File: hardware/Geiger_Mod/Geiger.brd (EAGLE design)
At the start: 52.1 x 28.6 mm, 19 parts, among them Q1 KSP44, Q2 2N3904

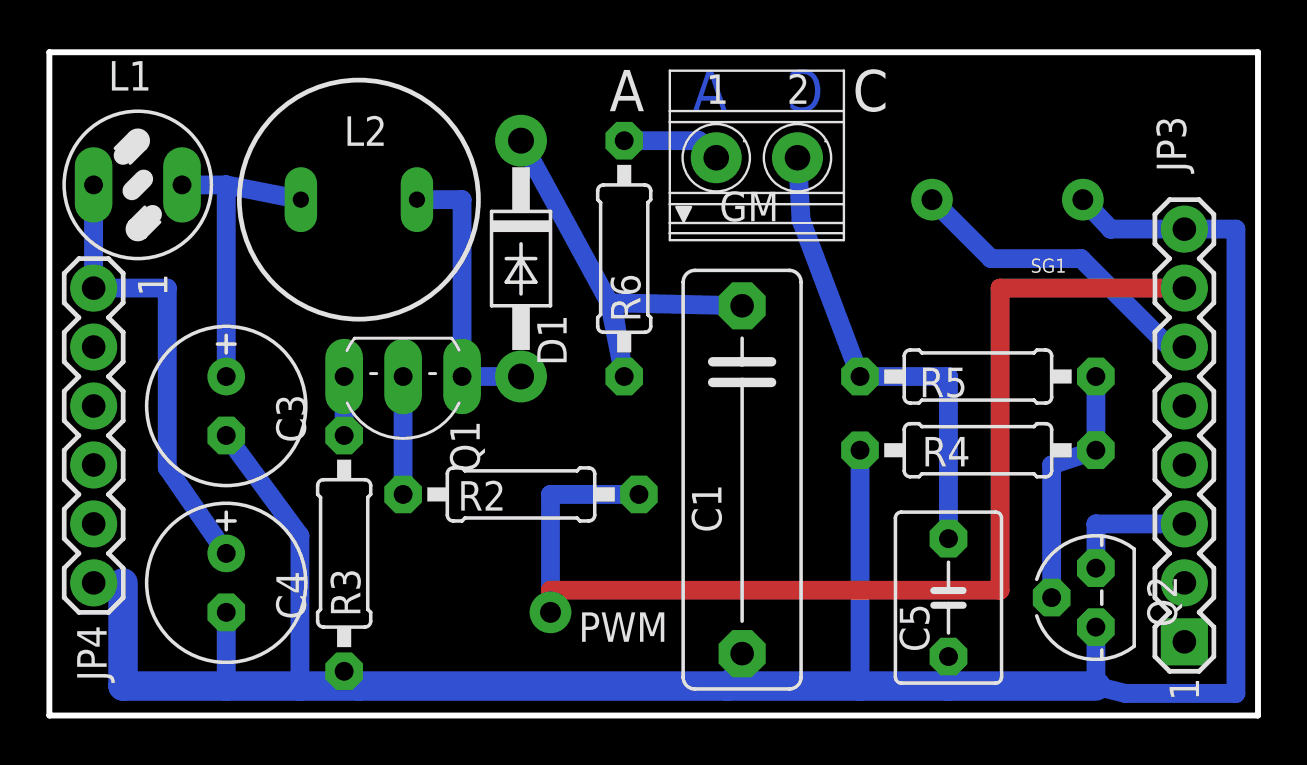
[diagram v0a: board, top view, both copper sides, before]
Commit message: Fixed Silk Screen for Q1 being wrong
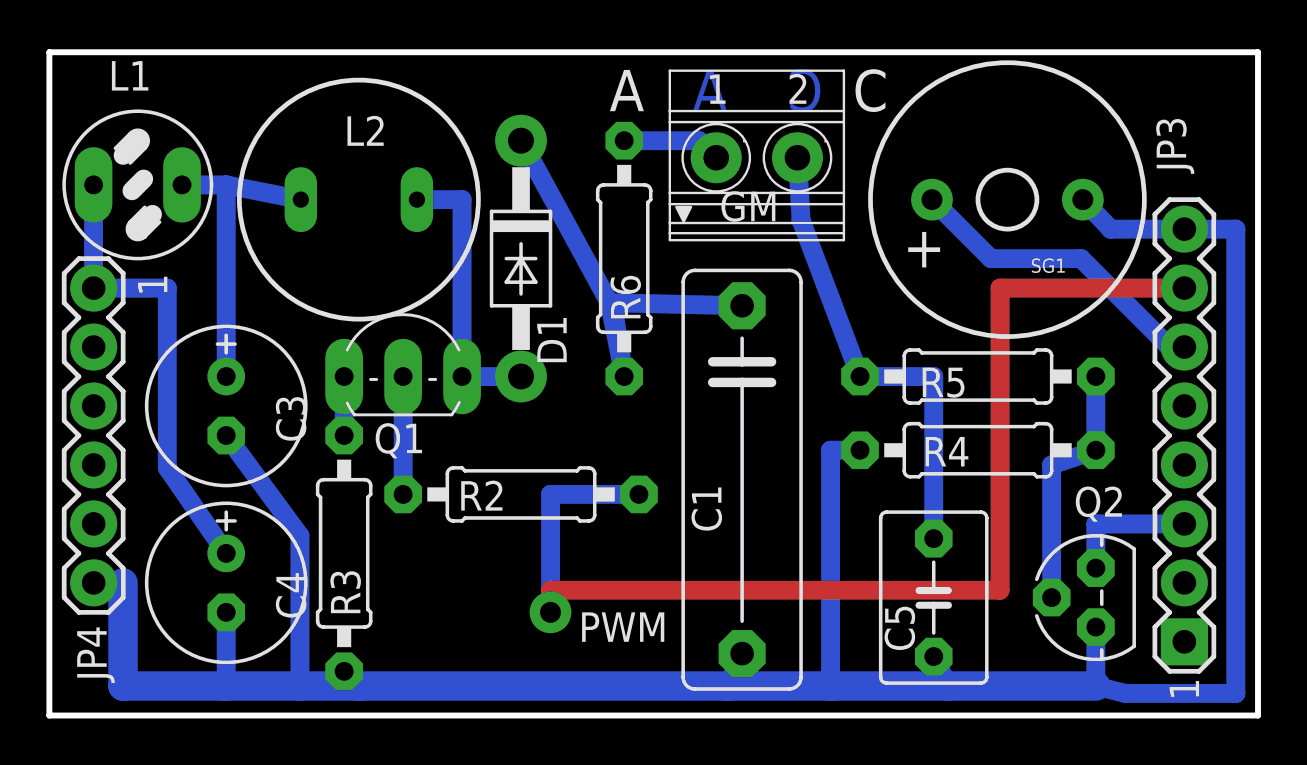
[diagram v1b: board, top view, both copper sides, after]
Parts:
- Q1: device transistor-npn:TO92-EBC -> transistor-npn:TO92-CBE
- moved Q1 1.27 mm to (21.6, 37.5), turned to 0 degrees
- moved C5 0.63 mm to (44.5, 27.9)
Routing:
- net GND: track 112.9 -> 114.3 mm
- net N$13: track 20.7 -> 20.1 mm
